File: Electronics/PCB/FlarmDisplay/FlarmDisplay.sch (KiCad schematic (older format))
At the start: 56 parts

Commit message: Initial schematic version complete
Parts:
- added BZ1: CMI-9705-0380-SMT-TR, symbol Device:Buzzer
- added D1: S1D-13-F, Diode_SMD:D_SMA, symbol Device:D
- added J2: SWD, Connector_PinHeader_2.54mm:PinHeader_1x04_P2.54mm_Vertical, symbol Connector:Conn_01x04_Male
- added R1: 200, Resistor_SMD:R_0805_2012Metric, symbol Device:R
- added R3, R4: 2K6, Resistor_SMD:R_0805_2012Metric, symbol Device:R
- added TP1: 3.3V, TestPoint:TestPoint_Pad_D2.0mm, symbol Connector:TestPoint
- added TP2: GND, TestPoint:TestPoint_Pad_D2.0mm, symbol Connector:TestPoint
- added U1: IPN80R3K3P7ATMA1, symbol FlarmDisplay:IPN80R3K3P7ATMA1
- C1, C10, C11, C12, C13, C14, C2, C3, C4, C5, C6, C7, C8: renamed from C?; footprint (none) -> Capacitor_SMD:C_0805_2012Metric
- D10, D11, D12, D13, D14, D15, D16, D17, D18, D19, D2, D20, D21, D22, D23, D24, D25, D26, D27, D28, D29, D3, D30, D31, D32, D33, D4, D5, D6, D7, D8, D9: renamed from D?; footprint (none) -> Diode_SMD:D_0805_2012Metric
- R2: renamed from R?; footprint (none) -> Resistor_SMD:R_0805_2012Metric
- SW1: renamed from SW?; value SW_Push -> RESET
- SW2: renamed from SW?; value SW_SPDT -> BOOT
- TP3, TP4: renamed from TP?; footprint (none) -> TestPoint:TestPoint_Pad_D2.0mm
- U3, U4: renamed from U?; footprint (none) -> Package_DFN_QFN:VQFN-24-1EP_4x4mm_P0.5mm_EP2.45x2.45mm
- Y1: renamed from Y?; footprint (none) -> Crystal:Crystal_SMD_3225-4Pin_3.2x2.5mm
- gave numbers to parts that had none: 3
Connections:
- net +3V3: now also BZ1.1 (-), D1.1 (K), J2.3 (Pin_3), TP1.1
- net GND: now also J2.4 (Pin_4), R3.2, R4.2, TP2.1, U1.3
- net BUZZER: now reaches U2.15 (PB0)
- net BUZZER: now also R1.2
- net at U3.20 (IREF): now also R3.1
- net at U4.20 (IREF): now also R4.1
- net JNTRST: no longer names the net of U2.27 (PB4)
- net JTCK renamed SWCLK
- net SWCLK: now also J2.2 (Pin_2)
- net JTDI: no longer names the net of U2.25 (PA15)
- net JTDO: no longer names the net of U2.26 (PB3)
- net JTMS renamed SWDAT
- net SWDAT: now also J2.1 (Pin_1)
- new net: BZ1.2 (+), D1.2 (A), U1.2
- new net: R1.1, U1.1
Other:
- note added: "BUZZER DRIVER"
- note added: "CONSTANT CURRENT SINK REFERENCE \nRESISTOR SET TO 2K6 FOR 20mA"
- note added: "INPUT"
- note added: "LED DRIVER"
- note added: "POWER FILTERING"
- moved on the sheet: C10, C11, C12, J1, R2, SW1, SW2, Y1

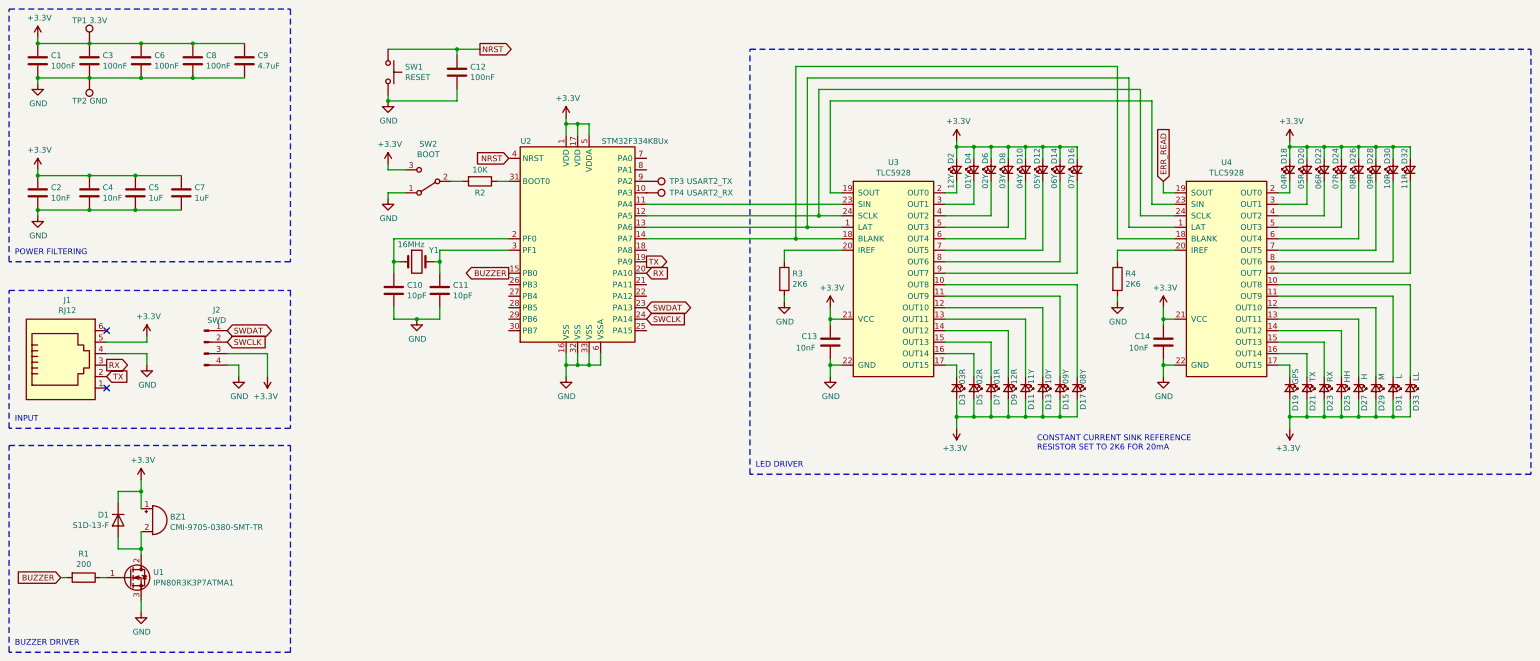
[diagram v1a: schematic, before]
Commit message: Started work on PCB, most placement done
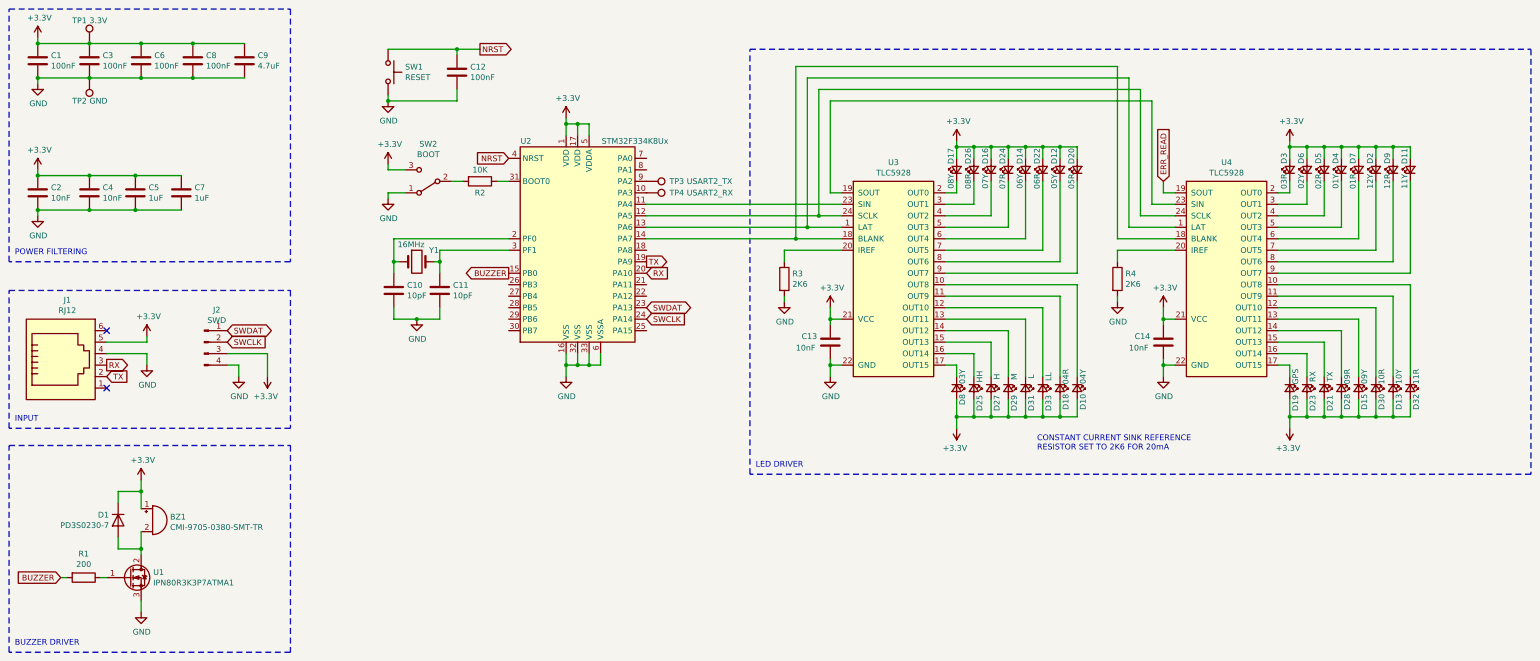
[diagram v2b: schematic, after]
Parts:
- BZ1: footprint (none) -> FlarmDisplay:CMI-9705-0380-SMT-TR
- C1, C10, C11, C12, C13, C14, C2, C3, C4, C5, C6, C7, C8: footprint Capacitor_SMD:C_0805_2012Metric -> Capacitor_SMD:C_0402_1005Metric
- C9: footprint (none) -> Capacitor_SMD:C_0805_2012Metric
- D1: value S1D-13-F -> PD3S0230-7; footprint Diode_SMD:D_SMA -> FlarmDisplay:POWERDI323
- D10, D11, D12, D13, D14, D15, D16, D17, D18, D19, D2, D20, D21, D22, D23, D24, D25, D26, D27, D28, D29, D3, D30, D31, D32, D33, D4, D5, D6, D7, D8, D9: footprint Diode_SMD:D_0805_2012Metric -> LED_SMD:LED_0805_2012Metric
- J1: footprint (none) -> Connector_RJ:RJ12_Amphenol_54601
- R1, R2, R3, R4: footprint Resistor_SMD:R_0805_2012Metric -> Resistor_SMD:R_0402_1005Metric
- SW1: footprint (none) -> FlarmDisplay:SMT_J
- SW2: footprint (none) -> FlarmDisplay:7814G-1-023E
- U1: footprint (none) -> Package_TO_SOT_SMD:SOT-323_SC-70
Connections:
- net at U3.10 (OUT8): now also D10.1 (K); no longer D17.1 (K)
- net at U3.11 (OUT9): now also D18.1 (K); no longer D15.1 (K)
- net at U3.12 (OUT10): now also D33.1 (K); no longer D13.1 (K)
- net at U3.13 (OUT11): now also D31.1 (K); no longer D11.1 (K)
- net at U3.14 (OUT12): now also D29.1 (K); no longer D9.1 (K)
- net at U3.15 (OUT13): now also D27.1 (K); no longer D7.1 (K)
- net at U3.16 (OUT14): now also D25.1 (K); no longer D5.1 (K)
- net at U3.17 (OUT15): now also D8.1 (K); no longer D3.1 (K)
- net at U3.2 (OUT0): now also D17.1 (K); no longer D2.1 (K)
- net at U3.3 (OUT1): now also D26.1 (K); no longer D4.1 (K)
- net at U3.4 (OUT2): now also D16.1 (K); no longer D6.1 (K)
- net at U3.5 (OUT3): now also D24.1 (K); no longer D8.1 (K)
- net at U3.6 (OUT4): now also D14.1 (K); no longer D10.1 (K)
- net at U3.7 (OUT5): now also D22.1 (K); no longer D12.1 (K)
- net at U3.8 (OUT6): now also D12.1 (K); no longer D14.1 (K)
- net at U3.9 (OUT7): now also D20.1 (K); no longer D16.1 (K)
- net at U4.10 (OUT8): now also D32.1 (K); no longer D33.1 (K)
- net at U4.11 (OUT9): now also D13.1 (K); no longer D31.1 (K)
- net at U4.12 (OUT10): now also D30.1 (K); no longer D29.1 (K)
- net at U4.13 (OUT11): now also D15.1 (K); no longer D27.1 (K)
- net at U4.14 (OUT12): now also D28.1 (K); no longer D25.1 (K)
- net at U4.15 (OUT13): now also D21.1 (K); no longer D23.1 (K)
- net at U4.16 (OUT14): now also D23.1 (K); no longer D21.1 (K)
- net at U4.2 (OUT0): now also D3.1 (K); no longer D18.1 (K)
- net at U4.3 (OUT1): now also D6.1 (K); no longer D20.1 (K)
- net at U4.4 (OUT2): now also D5.1 (K); no longer D22.1 (K)
- net at U4.5 (OUT3): now also D4.1 (K); no longer D24.1 (K)
- net at U4.6 (OUT4): now also D7.1 (K); no longer D26.1 (K)
- net at U4.7 (OUT5): now also D2.1 (K); no longer D28.1 (K)
- net at U4.8 (OUT6): now also D9.1 (K); no longer D30.1 (K)
- net at U4.9 (OUT7): now also D11.1 (K); no longer D32.1 (K)
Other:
- moved on the sheet: D10, D11, D12, D13, D14, D15, D16, D17, D18, D2, D20, D21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

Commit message: Latest
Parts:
- J1: footprint Connector_RJ:RJ12_Amphenol_54601 -> FlarmDisplay:RJE231660413T
- U1: footprint Package_TO_SOT_SMD:SOT-323_SC-70 -> Package_TO_SOT_SMD:SOT-223-3_TabPin2
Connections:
- net ERR_READ: no longer names the net of U4.19 (SOUT)
- no-connect marks 2 -> 14
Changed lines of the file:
@@
 F 0 "J1" H 1107 4267 50  0000 C CNN
 F 1 "RJ12" H 1107 4176 50  0000 C CNN
-F 2 "Connector_RJ:RJ12_Amphenol_54601" V 1050 3725 50  0001 C CNN
+F 2 "FlarmDisplay:RJE231660413T" V 1050 3725 50  0001 C CNN
 F 3 "~" V 1050 3725 50  0001 C CNN
 	1    1050 3700
@@
 Wire Wire Line
 	850  900  1300 900
-Wire Wire Line
-	850  1200 1300 1200
 $Comp
 L Device:C C3
@@
 	2200 1200 1750 1200
 $Comp
-L power:GND #PWR02
-U 1 1 6278A833
-P 850 1250
-F 0 "#PWR02" H 850 1000 50  0001 C CNN
-F 1 "GND" H 855 1077 50  0000 C CNN
-F 2 "" H 850 1250 50  0001 C CNN
-F 3 "" H 850 1250 50  0001 C CNN
-	1    850  1250
-	1    0    0    -1
-$EndComp
-$Comp
 L power:+3.3V #PWR01
 U 1 1 6278AA0E
@@
 	850  2050 850  2000
 Connection ~ 850  2050
-Wire Wire Line
-	850  1250 850  1200
-Connection ~ 850  1200
 Wire Wire Line
 	850  900  850  850
@@
 $EndComp
 Wire Wire Line
-	10650 3800 10650 3700
-Wire Wire Line
-	10650 3700 10750 3700
-Wire Wire Line
 	10650 3200 10650 3300
 Wire Wire Line
@@
 $EndComp
 Wire Wire Line
-	10650 3650 10650 3700
-Connection ~ 10650 3700
-Wire Wire Line
 	10650 3350 10650 3300
 Connection ~ 10650 3300
@@
 Wire Wire Line
 	10250 2600 10750 2600
-Text GLabel 10650 2100 1    50   Input ~ 0
-ERR_READ
-Wire Wire Line
-	10750 2200 10650 2200
-Wire Wire Line
-	10650 2200 10650 2100
 Text GLabel 6150 2800 2    50   Output ~ 0
 TX
@@
 F 0 "U1" H 1855 5596 50  0000 L CNN
 F 1 "IPN80R3K3P7ATMA1" H 1855 5505 50  0000 L CNN
-F 2 "Package_TO_SOT_SMD:SOT-323_SC-70" H 1800 5950 50  0001 C CNN
+F 2 "Package_TO_SOT_SMD:SOT-223-3_TabPin2" H 1800 5950 50  0001 C CNN
 F 3 "" H 1800 5950 50  0001 C CNN
 	1    1750 5550
@@
 	0    -1   -1   0
 $EndComp
+NoConn ~ 4950 3000
+NoConn ~ 4950 3100
+NoConn ~ 4950 3200
+NoConn ~ 4950 3300
+NoConn ~ 4950 3400
+NoConn ~ 6150 3400
+NoConn ~ 6150 3100
+NoConn ~ 6150 3000
+NoConn ~ 6150 2700
+NoConn ~ 6150 2000
+NoConn ~ 6150 1900
+NoConn ~ 10750 2200
+Wire Wire Line
+	10650 3650 10650 3700
+Wire Wire Line
+	10750 3700 10650 3700
+Connection ~ 10650 3700
+Wire Wire Line
+	10650 3700 10650 3800
+Wire Wire Line
+	850  1250 850  1200
+Wire Wire Line
+	850  1200 1300 1200
+Connection ~ 850  1200
+$Comp
+L power:GND #PWR02
+U 1 1 62A053B7
+P 850 1250
+F 0 "#PWR02" H 850 1000 50  0001 C CNN
+F 1 "GND" H 855 1077 50  0000 C CNN
+F 2 "" H 850 1250 50  0001 C CNN
+F 3 "" H 850 1250 50  0001 C CNN
+	1    850  1250
+	1    0    0    -1
+$EndComp
 $EndSCHEMATC
